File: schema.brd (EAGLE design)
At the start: 130 x 130 mm, 21 parts, among them IC3 HT7333, J1 FH12-24S-0.5SH(55), J3 C10418, U1 ESP-32S, U3 CH340ESMD

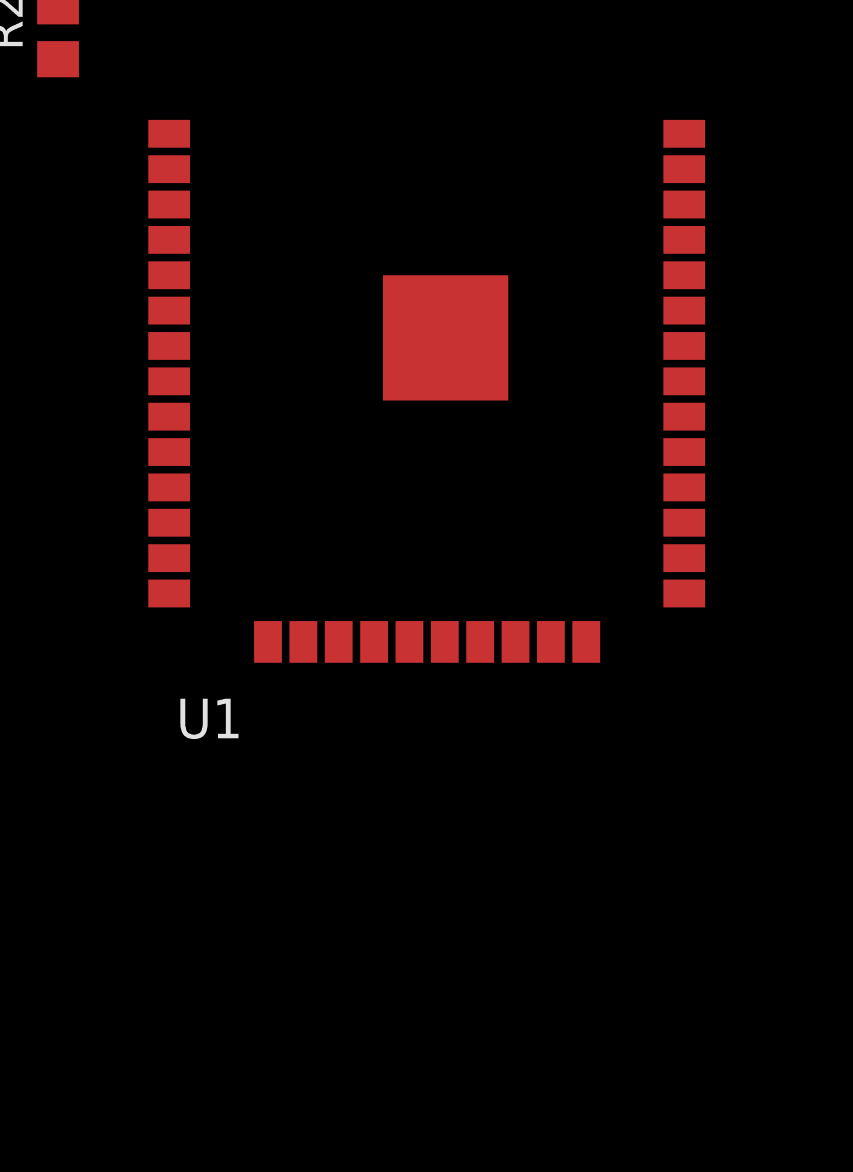
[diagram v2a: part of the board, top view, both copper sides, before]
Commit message: Added PSRAM
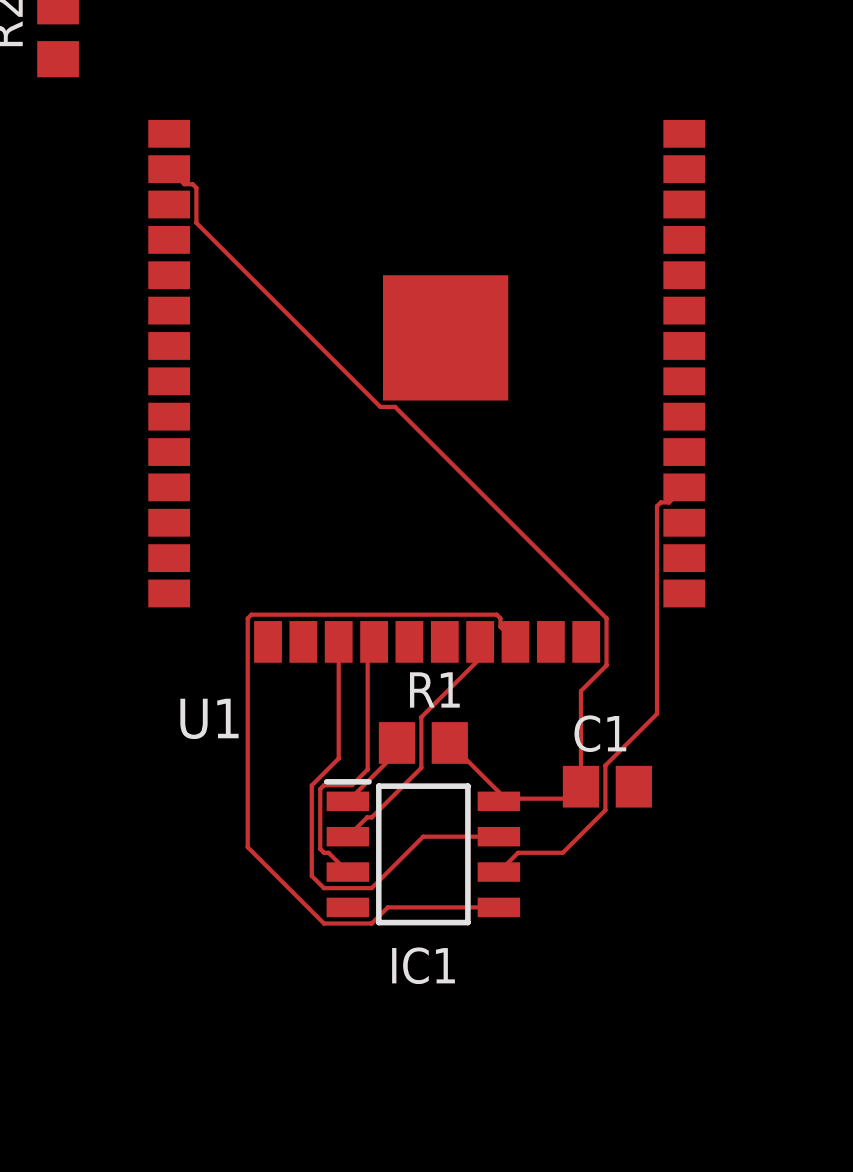
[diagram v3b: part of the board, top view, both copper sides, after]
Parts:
- added C1: 0.1uF, rcl:C0805
- added IC1: IPS6404L-SQ-SPN, water-lib:SOIC127P600X175-8N
- added R1: 10k, rcl:R0805
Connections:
- new net IO16: IC1.1, R1.1, U1.27
- new net PSRAM_CLK: IC1.6, U1.28
- new net SD0: IC1.2, U1.21
- new net SD1: IC1.5, U1.22
- new net SD2: IC1.7, U1.17
- new net SD3: IC1.3, U1.18
- net +3V3: now also C1.1, IC1.8, R1.2
- net GND: now also C1.2, IC1.4
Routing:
- net +3V3: track 0.04 -> 35.5 mm
- net SD1: track 0.00 -> 28.9 mm
- net PSRAM_CLK: track 0.00 -> 17.7 mm
- net SD2: track 0.00 -> 16.5 mm
- net SD3: track 0.00 -> 10.2 mm
- net SD0: track 0.00 -> 9.06 mm
- net IO16: track 0.00 -> 2.82 mm
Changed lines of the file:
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@@
 <drawing>
 <settings>
-<setting alwaysvectorfont="yes"/>
+<setting alwaysvectorfont="no"/>
 <setting verticaltext="up"/>
 </settings>
@@
 <attribute name="RS_PRICE-STOCK" value="" x="-39" y="13" size="1.778" layer="27" display="off"/>
 </element>
+<element name="IC1" library="water-lib" package="SOIC127P600X175-8N" value="IPS6404L-SQ-SPN" x="63" y="80" smashed="yes">
+<attribute name="DESCRIPTION" value="int" x="63" y="80" size="1.778" layer="27" display="off"/>
+<attribute name="HEIGHT" value="1.75mm" x="63" y="80" size="1.778" layer="27" display="off"/>
+<attribute name="MANUFACTURER_NAME" value="Electrodragon" x="63" y="80" size="1.778" layer="27" display="off"/>
+<attribute name="MANUFACTURER_PART_NUMBER" value="IPS6404L-SQ-SPN" x="63" y="80" size="1.778" layer="27" display="off"/>
+<attribute name="MOUSER_PART_NUMBER" value="" x="63" y="80" size="1.778" layer="27" display="off"/>
+<attribute name="MOUSER_PRICE-STOCK" value="" x="63" y="80" size="1.778" layer="27" display="off"/>
+<attribute name="NAME" x="63" y="76" size="1.27" layer="25" align="center"/>
+<attribute name="RS_PART_NUMBER" value="" x="63" y="80" size="1.778" layer="27" display="off"/>
+<attribute name="RS_PRICE-STOCK" value="" x="63" y="80" size="1.778" layer="27" display="off"/>
+<attribute name="VALUE" x="63" y="84" size="1.27" layer="27" align="center"/>
+</element>
+<element name="R1" library="rcl" library_urn="urn:adsk.eagle:library:334" package="R0805" package3d_urn="urn:adsk.eagle:package:23553/2" value="10k" x="63" y="84" smashed="yes">
+<attribute name="NAME" x="62.365" y="85.27" size="1.27" layer="25"/>
+<attribute name="POPULARITY" value="86" x="63" y="84" size="1.778" layer="27" display="off"/>
+<attribute name="SPICEPREFIX" value="R" x="63" y="84" size="1.778" layer="27" display="off"/>
+<attribute name="VALUE" x="62.365" y="81.46" size="1.27" layer="27"/>
+</element>
+<element name="C1" library="rcl" library_urn="urn:adsk.eagle:library:334" package="C0805" package3d_urn="urn:adsk.eagle:package:23617/2" value="0.1uF" x="69.61" y="82.43" smashed="yes">
+<attribute name="NAME" x="68.34" y="83.7" size="1.27" layer="25"/>
+<attribute name="POPULARITY" value="88" x="69.61" y="82.43" size="1.778" layer="27" display="off"/>
+<attribute name="SPICEPREFIX" value="C" x="69.61" y="82.43" size="1.778" layer="27" display="off"/>
+<attribute name="VALUE" x="68.34" y="79.89" size="1.27" layer="27"/>
+</element>
 </elements>
 <signals>
@@
 <contactref element="R2" pad="2"/>
 <wire x1="53.84" y1="104.64" x2="53.87" y2="104.61" width="0.1524" layer="1"/>
+<contactref element="R1" pad="2"/>
+<contactref element="IC1" pad="8"/>
+<contactref element="C1" pad="1"/>
+<wire x1="63.95" y1="84" x2="65.712" y2="82.238" width="0.1524" layer="1"/>
+<wire x1="65.712" y1="82.238" x2="65.712" y2="82" width="0.1524" layer="1"/>
+<wire x1="65.712" y1="82" x2="65.712" y2="81.905" width="0.1524" layer="1"/>
+<wire x1="68.615" y1="82.385" x2="68.23" y2="82" width="0.1524" layer="1"/>
+<wire x1="68.23" y1="82" x2="65.712" y2="82" width="0.1524" layer="1"/>
+<wire x1="69.5786" y1="86.7853125" x2="69.5786" y2="88.4746875" width="0.1524" layer="1"/>
+<wire x1="54.8486" y1="103.9346875" x2="54.7146875" y2="104.0686" width="0.1524" layer="1"/>
+<wire x1="54.7146875" y1="104.0686" x2="54.4114" y2="104.0686" width="0.1524" layer="1"/>
+<wire x1="54.4114" y1="104.0686" x2="53.87" y2="104.61" width="0.1524" layer="1"/>
+<wire x1="69.5786" y1="86.7853125" x2="68.66" y2="85.8667125" width="0.1524" layer="1"/>
+<wire x1="61.9818875" y1="96.0714" x2="61.4553125" y2="96.0714" width="0.1524" layer="1"/>
+<wire x1="69.5786" y1="88.4746875" x2="61.9818875" y2="96.0714" width="0.1524" layer="1"/>
+<wire x1="61.4553125" y1="96.0714" x2="54.8486" y2="102.6781125" width="0.1524" layer="1"/>
+<wire x1="54.8486" y1="102.6781125" x2="54.8486" y2="103.9346875" width="0.1524" layer="1"/>
+<wire x1="68.66" y1="82.43" x2="68.615" y2="82.385" width="0.1524" layer="1"/>
+<wire x1="68.66" y1="85.8667125" x2="68.66" y2="82.43" width="0.1524" layer="1"/>
 <wire x1="53.84" y1="104.64" x2="49.88" y2="110.46" width="0" layer="19" extent="1-1"/>
 </signal>
@@
 <contactref element="C10" pad="2"/>
 <contactref element="U1" pad="GND"/>
-<wire x1="72.37" y1="105.88" x2="63.8" y2="98.55" width="0" layer="19" extent="1-1"/>
+<contactref element="IC1" pad="4"/>
+<contactref element="C1" pad="2"/>
+<wire x1="57.42" y1="87.63" x2="60.288" y2="78.095" width="0" layer="19" extent="1-1"/>
+<wire x1="70.56" y1="82.43" x2="60.288" y2="78.095" width="0" layer="19" extent="1-1"/>
 </signal>
 <signal name="EN">
@@
 <via x="5.205925" y="51.554075" extent="1-16" drill="0.35"/>
 </signal>
+<signal name="IO16">
+<contactref element="IC1" pad="1"/>
+<contactref element="R1" pad="1"/>
+<contactref element="U1" pad="27"/>
+<wire x1="60.288" y1="81.905" x2="62.05" y2="83.667" width="0.1524" layer="1"/>
+<wire x1="62.05" y1="83.667" x2="62.05" y2="84" width="0.1524" layer="1"/>
+<wire x1="62.05" y1="84" x2="72.37" y2="91.91" width="0" layer="19" extent="1-1"/>
+</signal>
+<signal name="SD0">
+<contactref element="IC1" pad="2"/>
+<contactref element="U1" pad="21"/>
+<wire x1="60.288" y1="80.635" x2="60.9794" y2="81.3264" width="0.1524" layer="1"/>
+<wire x1="60.9794" y1="81.3264" x2="61.1451875" y2="81.3264" width="0.1524" layer="1"/>
+<wire x1="61.1451875" y1="81.3264" x2="62.9286" y2="83.1098125" width="0.1524" layer="1"/>
+<wire x1="62.9286" y1="83.1098125" x2="62.9286" y2="84.9286" width="0.1524" layer="1"/>
+<wire x1="65.04" y1="87.04" x2="65.04" y2="87.63" width="0.1524" layer="1"/>
+<wire x1="62.9286" y1="84.9286" x2="65.04" y2="87.04" width="0.1524" layer="1"/>
+</signal>
+<signal name="SD3">
+<contactref element="IC1" pad="3"/>
+<contactref element="U1" pad="18"/>
+<wire x1="59.4308125" y1="80.0564" x2="59.2969" y2="80.1903125" width="0.1524" layer="1"/>
+<wire x1="59.2969" y1="82.3496875" x2="59.4308125" y2="82.4836" width="0.1524" layer="1"/>
+<wire x1="59.4308125" y1="82.4836" x2="60.43554375" y2="82.4836" width="0.1524" layer="1"/>
+<wire x1="60.288" y1="79.365" x2="59.5966" y2="80.0564" width="0.1524" layer="1"/>
+<wire x1="59.5966" y1="80.0564" x2="59.4308125" y2="80.0564" width="0.1524" layer="1"/>
+<wire x1="59.2969" y1="80.1903125" x2="59.2969" y2="82.3496875" width="0.1524" layer="1"/>
+<wire x1="61" y1="87.4" x2="61.23" y2="87.63" width="0.1524" layer="1"/>
+<wire x1="60.43554375" y1="82.4836" x2="61" y2="83.04805625" width="0.1524" layer="1"/>
+<wire x1="61" y1="83.04805625" x2="61" y2="87.4" width="0.1524" layer="1"/>
+</signal>
+<signal name="SD1">
+<contactref element="IC1" pad="5"/>
+<contactref element="U1" pad="22"/>
+<wire x1="61.1451875" y1="77.5164" x2="59.4308125" y2="77.5164" width="0.1524" layer="1"/>
+<wire x1="56.6914" y1="88.4746875" x2="56.8253125" y2="88.6086" width="0.1524" layer="1"/>
+<wire x1="65.6346875" y1="88.6086" x2="65.7686" y2="88.4746875" width="0.1524" layer="1"/>
+<wire x1="56.8253125" y1="88.6086" x2="65.6346875" y2="88.6086" width="0.1524" layer="1"/>
+<wire x1="65.7686" y1="88.4746875" x2="65.7686" y2="88.1714" width="0.1524" layer="1"/>
+<wire x1="65.7686" y1="88.1714" x2="66.31" y2="87.63" width="0.1524" layer="1"/>
+<wire x1="65.712" y1="78.095" x2="61.7237875" y2="78.095" width="0.1524" layer="1"/>
+<wire x1="61.7237875" y1="78.095" x2="61.1451875" y2="77.5164" width="0.1524" layer="1"/>
+<wire x1="59.4308125" y1="77.5164" x2="56.6914" y2="80.2558125" width="0.1524" layer="1"/>
+<wire x1="56.6914" y1="80.2558125" x2="56.6914" y2="88.4746875" width="0.1524" layer="1"/>
+</signal>
+<signal name="SD2">
+<contactref element="IC1" pad="7"/>
+<contactref element="U1" pad="17"/>
+<wire x1="61.1451875" y1="78.7864" x2="59.4308125" y2="78.7864" width="0.1524" layer="1"/>
+<wire x1="58.9921" y1="82.47594375" x2="59.96" y2="83.44384375" width="0.1524" layer="1"/>
+<wire x1="59.96" y1="83.44384375" x2="59.96" y2="87.63" width="0.1524" layer="1"/>
+<wire x1="59.4308125" y1="78.7864" x2="58.9921" y2="79.2251125" width="0.1524" layer="1"/>
+<wire x1="58.9921" y1="79.2251125" x2="58.9921" y2="82.47594375" width="0.1524" layer="1"/>
+<wire x1="65.712" y1="80.635" x2="62.9937875" y2="80.635" width="0.1524" layer="1"/>
+<wire x1="62.9937875" y1="80.635" x2="61.1451875" y2="78.7864" width="0.1524" layer="1"/>
+</signal>
+<signal name="PSRAM_CLK">
+<contactref element="IC1" pad="6"/>
+<contactref element="U1" pad="28"/>
+<wire x1="65.712" y1="79.365" x2="66.4034" y2="80.0564" width="0.1524" layer="1"/>
+<wire x1="69.5386" y1="81.5853125" x2="69.5386" y2="83.1916" width="0.1524" layer="1"/>
+<wire x1="71.3914" y1="92.5046875" x2="71.5253125" y2="92.6386" width="0.1524" layer="1"/>
+<wire x1="71.5253125" y1="92.6386" x2="71.8286" y2="92.6386" width="0.1524" layer="1"/>
+<wire x1="71.8286" y1="92.6386" x2="72.37" y2="93.18" width="0.1524" layer="1"/>
+<wire x1="69.5386" y1="83.1916" x2="71.3914" y2="85.0444" width="0.1524" layer="1"/>
+<wire x1="71.3914" y1="85.0444" x2="71.3914" y2="92.5046875" width="0.1524" layer="1"/>
+<wire x1="66.4034" y1="80.0564" x2="68.0096875" y2="80.0564" width="0.1524" layer="1"/>
+<wire x1="68.0096875" y1="80.0564" x2="69.5386" y2="81.5853125" width="0.1524" layer="1"/>
+</signal>
 </signals>

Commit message: CAM ribbon connection
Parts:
- added C2: 15uF, rcl:C0805
- added C3, C5: 0.1uF, rcl:C0805
- added R10, R11, R9: 4k7, rcl:R0805
- added R12, R3: 10k, rcl:R0805
- added R4: 1k, rcl:R0805
- added S2: (no value), switch-omron:B3F-10XX
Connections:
- new net +1V2: J1.15
- new net +2V8: J1.21
- new net CAM_RST: C5.2, J1.19, R9.1
- new net CSI_D0: J1.6, U1.29
- new net CSI_D1: J1.4, U1.30
- new net CSI_D2: J1.3, U1.31
- new net CSI_D3: J1.5, U1.33
- new net CSI_D4: J1.7, U1.4
- new net CSI_D5: J1.9, U1.5
- new net CSI_D6: J1.11, U1.6
- new net CSI_D7: J1.13, U1.7
- new net CSI_HSYNC: J1.16, U1.37
- new net CSI_MCLK: J1.12, R3.1, U1.26
- new net CSI_PCLK: C2.1, J1.8, U1.36
- new net CSI_VSYNC: J1.18, U1.10
- new net IO0: R12.2, S2.3, S2.4, U1.25
- new net N$1: J1.17, R4.1
- new net NC@1: J1.24
- new net NC@2: J1.1
- new net NC@3: J1.2
- new net TWI_SCK: J1.20, R10.2, U1.12
- new net TWI_SDA: J1.22, R11.1, U1.11
- net +3V3: now also C3.1, J1.14, R10.1, R11.2, R12.1, R3.2, R9.2
- net GND: now also C2.2, C3.2, C5.1, J1.10, J1.23, R4.2, S2.1, S2.2
